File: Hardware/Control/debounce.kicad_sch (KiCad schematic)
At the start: 22 parts, among them U3 SN74HCS244QPWRQ1

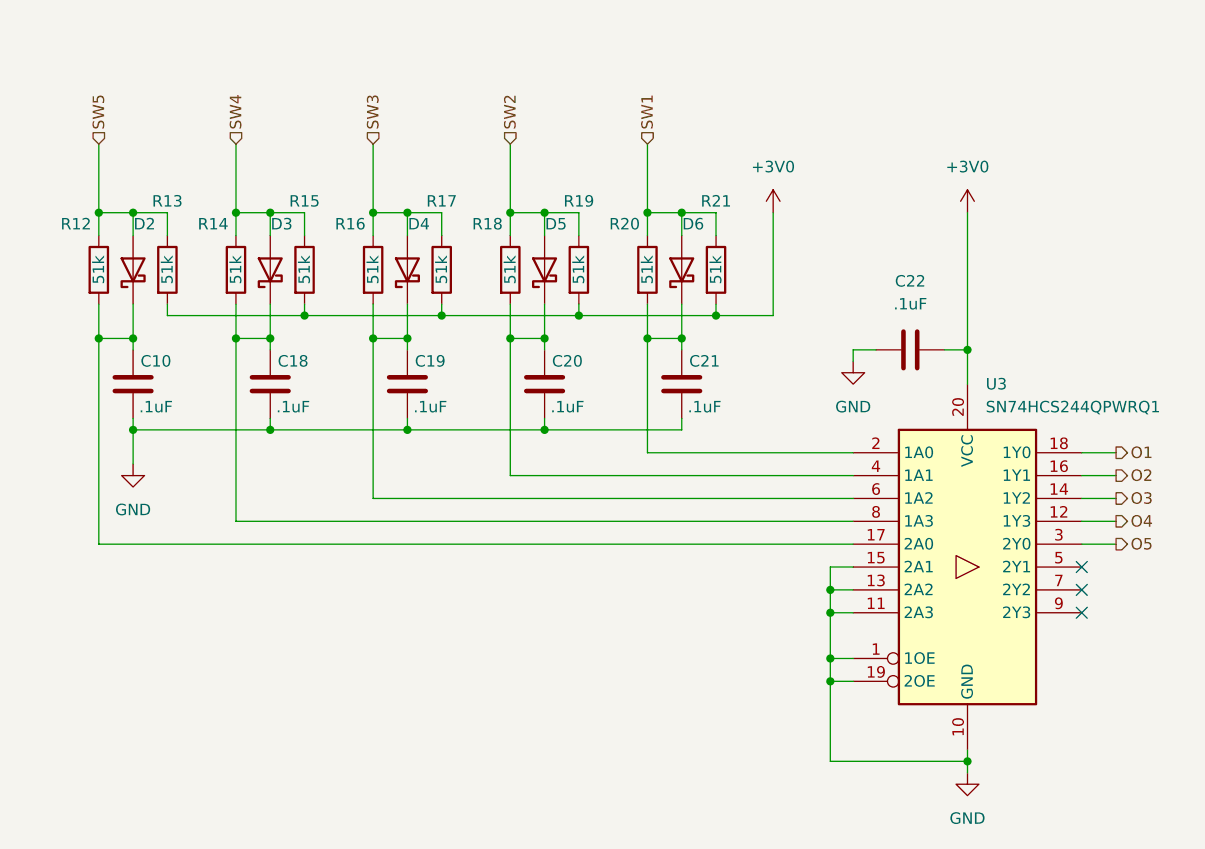
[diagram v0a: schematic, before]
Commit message: Move to AVR128DB64 MCU
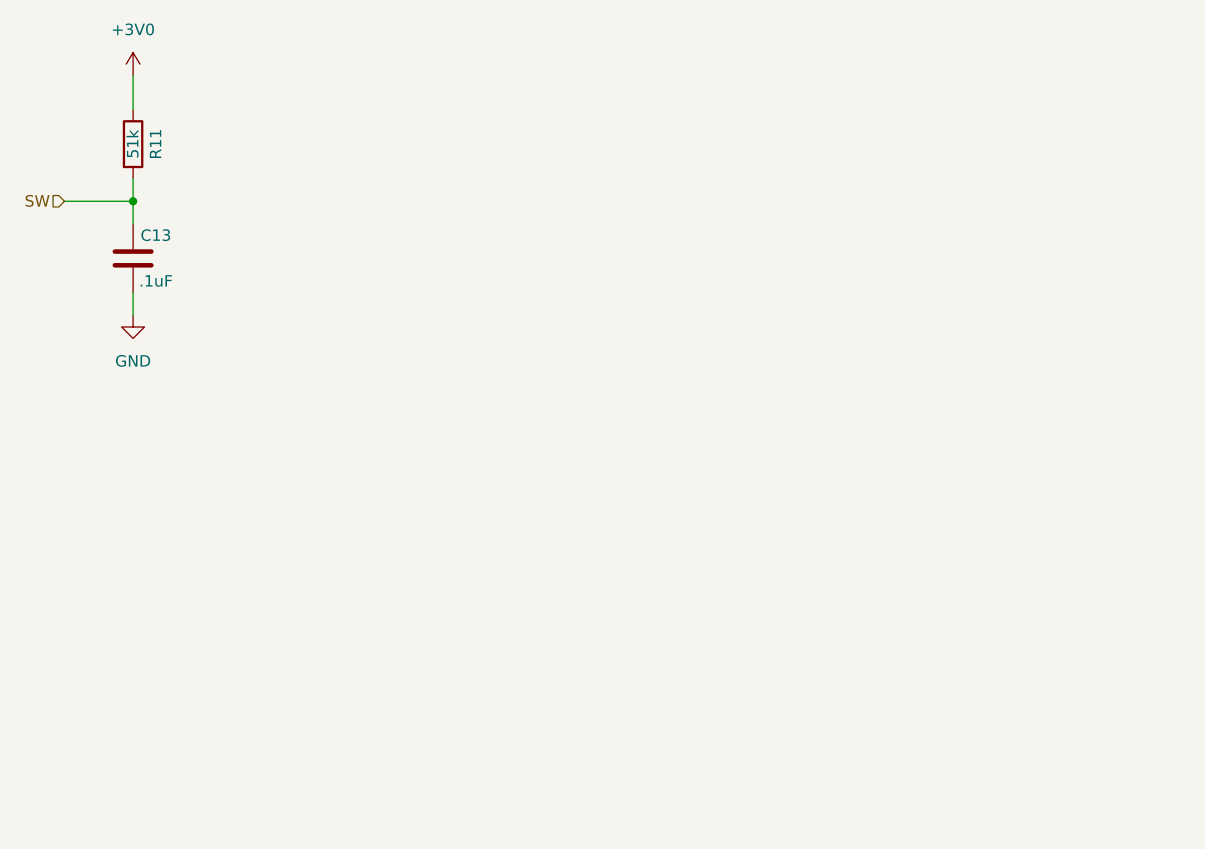
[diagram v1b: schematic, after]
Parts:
- removed C18, C19, C20, C21, C22: .1uF, Capacitor_SMD:C_0805_2012Metric, symbol Device:C
- removed D2, D3, D4, D5, D6: RB886CST2RA, Diode_SMD:D_SOD-923, symbol Device:D_Schottky
- removed R12, R14, R15, R16, R17, R18, R19, R20, R21: 51k, Resistor_SMD:R_0805_2012Metric, symbol Device:R
- removed U3: SN74HCS244QPWRQ1, Package_SO:TSSOP-20_4.4x6.5mm_P0.65mm, symbol 74xx:74AHC244
- C13: renamed from C10; Product Number (none) -> CGA4J2X8R1H104K125AE
- R11: renamed from R13; Product Number (none) -> ERJ-6ENF5102V
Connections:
- net SW5 is gone; now on net +3V0: R11.1
- net +3V0: no longer R11.2
- net SW: now reaches C13.1
- net SW: now also R11.2
- no-connect marks 3 -> 0
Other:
- moved on the sheet: C13, R11
